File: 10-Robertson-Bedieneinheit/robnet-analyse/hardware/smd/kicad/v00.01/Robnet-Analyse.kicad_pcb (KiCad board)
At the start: 2 copper layers, 100 x 100 mm, 71 parts, among them J1 MSTBA 6-pol., J2 MSTBA 2-pol., J3 MSTBA 6-pol., J4 Messpunkte, J5 Raspberry Pi Zero 2 W, U1 MAX3488EEPA, U2 MCP3208-CI/P, U3 R-78B5.0-2.0, U4 LM4040AIZ-2.5, U6 MCP3208-CI/P

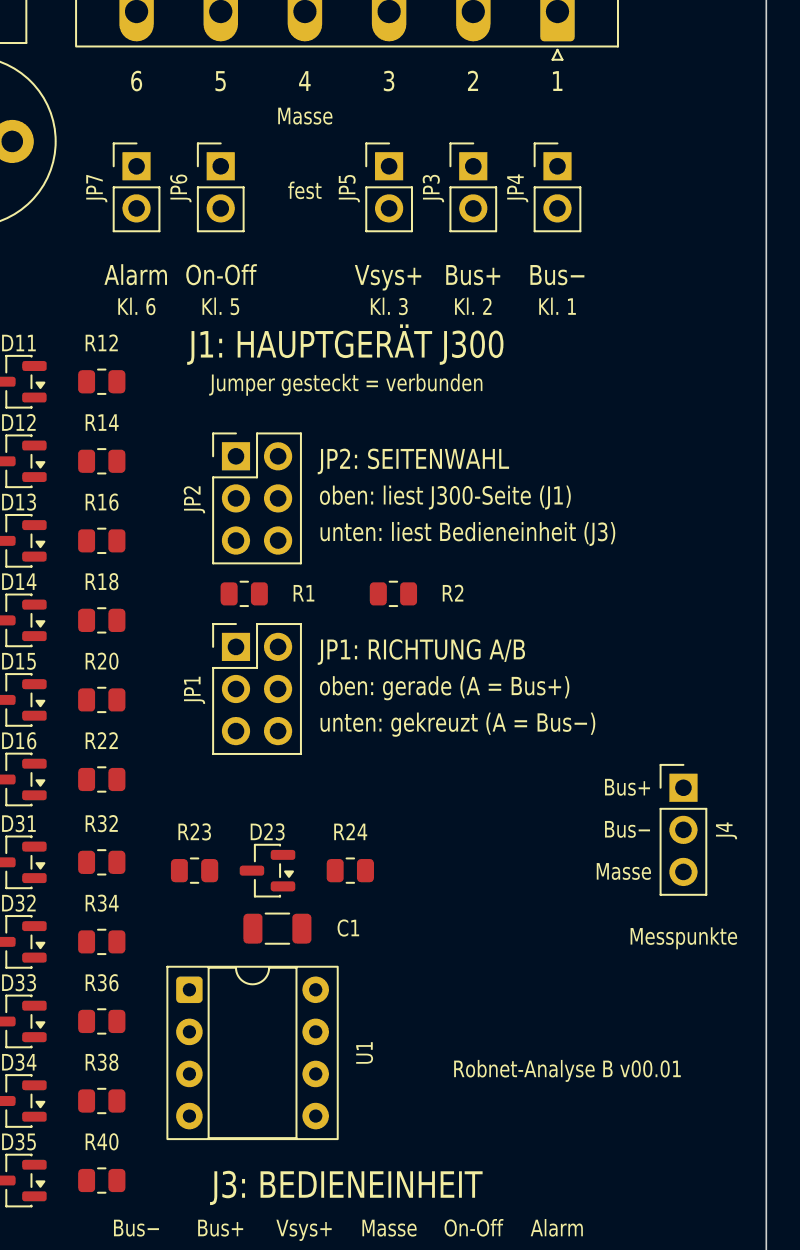
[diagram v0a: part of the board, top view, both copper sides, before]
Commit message: Robnet-Analyse Linie B: Aufdruck JP1/JP2 mit Stellungen A-E, Klemmennamen J1, Hersteller
- Jumper_JP1_JP2.html 00.01: alle Stellungen von JP1/JP2 (A-E) und falsche Steckungen
- Platine: Stiftreihen von JP1/JP2 beschriftet, Bildtabelle A-E und "nie quer",
  Klemmennamen an J1, "SuAn electronic" / "Lutz Pestel, 2026"
- Bauteilauswahl SMD 00.10, CLAUDE.md: Obergrenze 300 fuer die HTML-Seite

Co-Authored-By: Claude Opus 5.5 <noreply@anthropic.com>
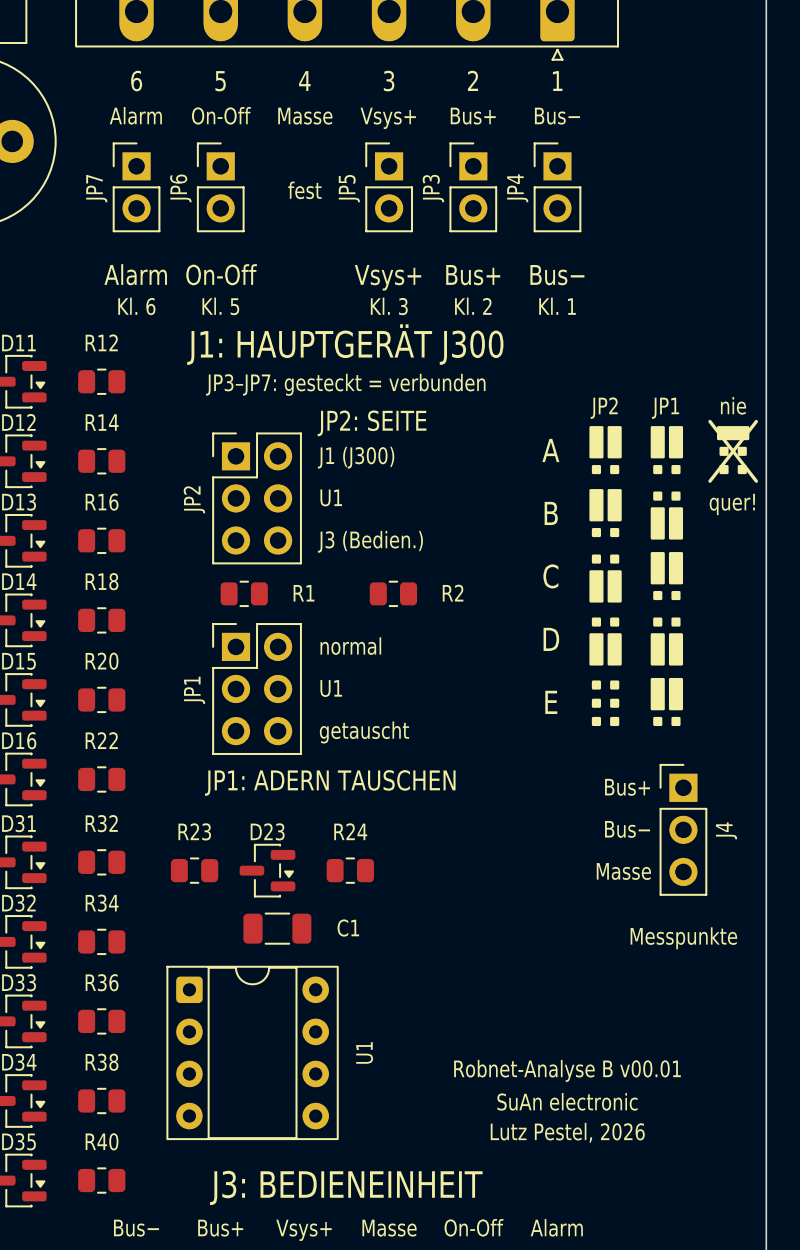
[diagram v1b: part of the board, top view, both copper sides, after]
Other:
- board text added: "A"
- board text added: "B"
- board text added: "C"
- board text added: "D"
- board text added: "E"
- board text added: "J1 (J300)"
- board text added: "J3 (Bedien.)"
- board text added: "JP1"
- board text added: "JP1: ADERN TAUSCHEN"
- board text added: "JP2"
- board text added: "JP2: SEITE"
- board text added: "JP3–JP7: gesteckt = verbunden"
- board text added: "Lutz Pestel, 2026"
- board text added: "SuAn electronic"
- board text added: "U1"
- board text added: "getauscht"
- board text added: "nie"
- board text added: "normal"
- board text added: "quer!"
- board text removed: "JP1: RICHTUNG A/B"
- board text removed: "JP2: SEITENWAHL"
- board text removed: "Jumper gesteckt = verbunden"
- board text removed: "oben: gerade (A = Bus+)"
- board text removed: "oben: liest J300-Seite (J1)"
- board text removed: "unten: gekreuzt (A = Bus−)"
- board text removed: "unten: liest Bedieneinheit (J3)"

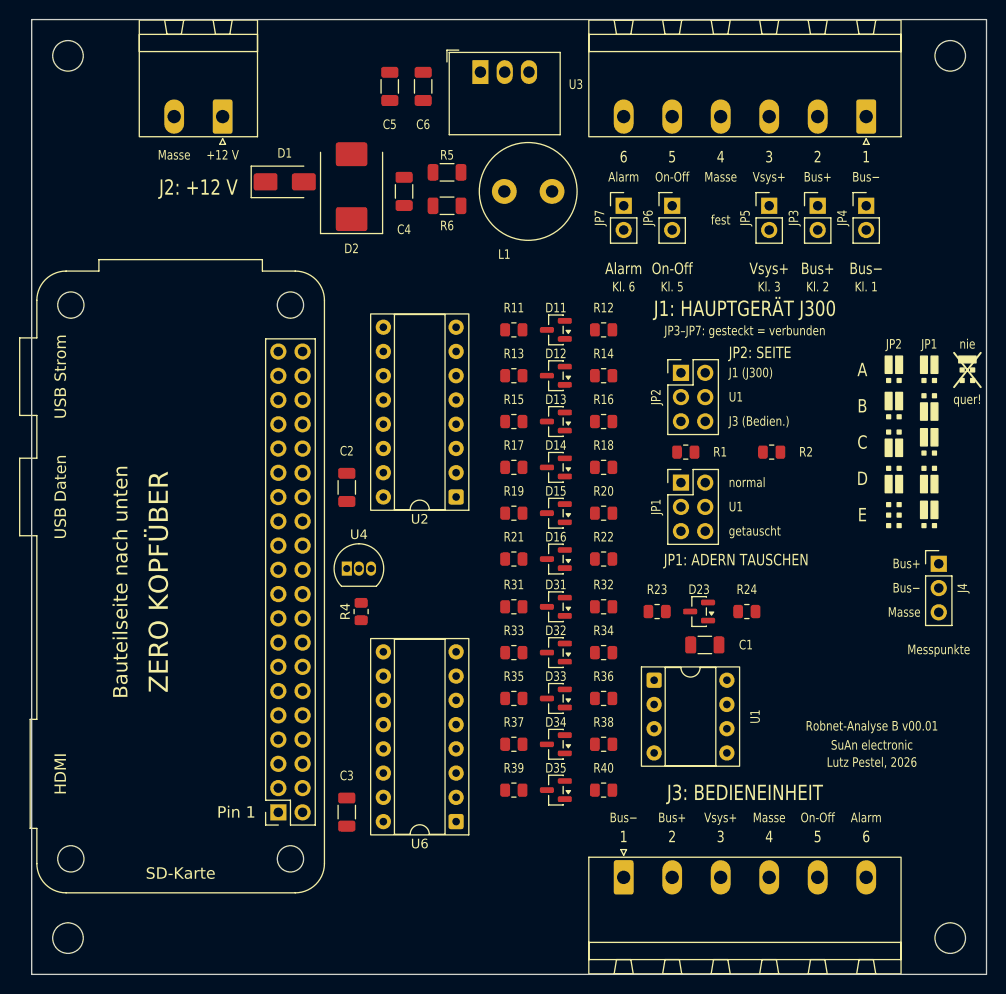
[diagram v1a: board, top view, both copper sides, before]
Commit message: Robnet-Analyse Linie B: Leiterbahnen Gruppe 1 (Versorgung und Masse)
- bahnen_erzeugen/robnet_bahnen.py 00.01: liest die platzierte Platine, ergaenzt Bahnen,
  bricht bei in KiCad verschobenen Teilen oder gezeichneten Bahnen ab
- Platzierungsskript 00.03 schreibt Zwischendatei Robnet-Analyse_platziert.kicad_pcb
  mit denselben Regeln; Projektdatei bleibt beim Speichern erhalten
- Gruppe 1: 12 V, 5 V aussen herum, 3,3 V unten mit Durchkontaktierung je BAT54S,
  Masseflaeche unten; DRC ohne Fehler, Abgleich 0; R21 (+12V_F) mit Gruppe 3
- Konzept 00.39, Bauteilauswahl SMD 00.11

Co-Authored-By: Claude Opus 5.5 <noreply@anthropic.com>
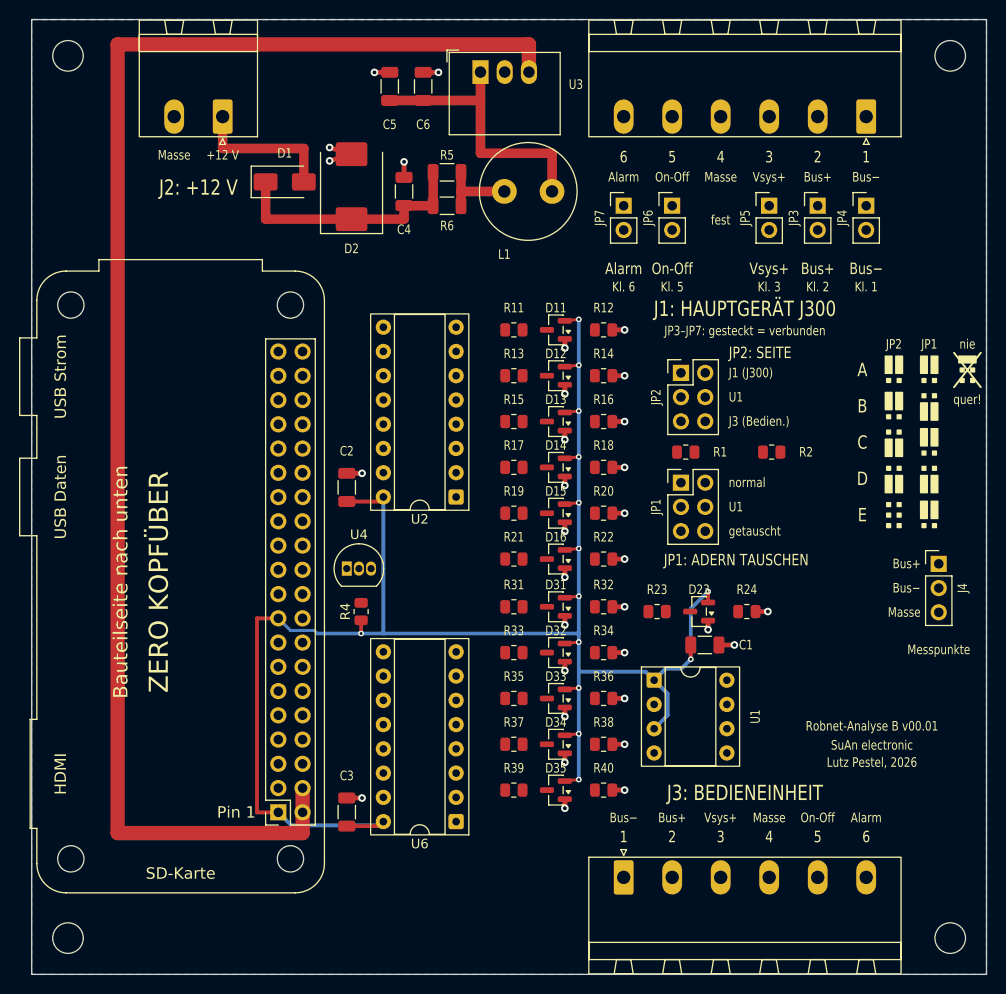
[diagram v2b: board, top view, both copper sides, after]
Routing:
- net /Bus-Empfänger/+3V3: track 0.00 -> 185.9 mm, vias 0 -> 14
- net /Rechner/+5V: track 0.00 -> 152.7 mm
- net GND: track 0.00 -> 41.3 mm, vias 0 -> 32
- net Net-(U3-IN): track 0.00 -> 29.5 mm
- net /Messung (Teiler, Wandler)/+12V_F: track 0.00 -> 26.3 mm
- net /Versorgung/+12V_EIN: track 0.00 -> 15.3 mm
- net Net-(L1-Pad1): track 0.00 -> 8.04 mm
- added copper zone on B.Cu, net GND

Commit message: Robnet-Analyse Linie B: Leiterbahnen Gruppe 2 (Adern J1 -> Jumper -> J3)
- Platzierung 00.04: R31-R39 um 180 Grad (Ader aussen), Kanalzeilen in Kanalfolge
  der Wandler (CH0 unten)
- Bahnen 00.02: Seite J300 ueber J1 und durch die Gasse zu den Teilern, Seite
  Bedieneinheit rechts herum und in Boegen unter J3 durch (keine Kreuzung trotz
  gespiegelter Klemmen); JP2, J4, R23, R21; 11 Durchkontaktierungen
- 3,3 V unten zwischen die Kanalbloecke verlegt; Schalter --neue-lage
- DRC ohne Fehler, Abgleich 0; Konzept 00.40, Bauteilauswahl SMD 00.12

Co-Authored-By: Claude Opus 5.5 <noreply@anthropic.com>
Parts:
- moved D11 24.0 mm to (54.9, 56.5)
- moved D16 24.0 mm to (54.9, 32.5)
- moved R11 24.0 mm to (50.5, 56.5)
- moved R12 24.0 mm to (59.9, 56.5)
- moved R21 24.0 mm to (50.5, 32.5)
- moved R22 24.0 mm to (59.9, 32.5)
- moved D31 19.2 mm to (54.9, 80.7)
- moved D35 19.2 mm to (54.9, 61.5)
- moved R31 19.2 mm to (50.5, 80.7), turned to 180 degrees
- moved R32 19.2 mm to (59.9, 80.7)
- moved R39 19.2 mm to (50.5, 61.5), turned to 180 degrees
- moved R40 19.2 mm to (59.9, 61.5)
- moved D12 14.4 mm to (54.9, 51.7)
- moved D15 14.4 mm to (54.9, 37.3)
- moved R13 14.4 mm to (50.5, 51.7)
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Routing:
- net /Bus-Empfänger/BUSN_J: track 0.00 -> 189.4 mm, vias 0 -> 2
- net /Bus-Empfänger/BUSN_B: track 0.00 -> 187.2 mm, vias 0 -> 1
- net /Bus-Empfänger/BUSP_B: track 0.00 -> 186.9 mm, vias 0 -> 1
- net /Bus-Empfänger/BUSP_J: track 0.00 -> 185.5 mm
- net /Messung (Teiler, Wandler)/ALARM_B: track 0.00 -> 157.4 mm, vias 0 -> 2
- net /Messung (Teiler, Wandler)/ONOFF_B: track 0.00 -> 153.2 mm, vias 0 -> 2
- net /Messung (Teiler, Wandler)/VSYS_B: track 0.00 -> 141.8 mm
- net /Messung (Teiler, Wandler)/ALARM_J: track 0.00 -> 107.8 mm, vias 0 -> 1
- net /Messung (Teiler, Wandler)/VSYS_J: track 0.00 -> 93.9 mm
- net /Messung (Teiler, Wandler)/ONOFF_J: track 0.00 -> 76.5 mm
- net /Messung (Teiler, Wandler)/+12V_F: track 26.3 -> 43.4 mm, vias 0 -> 2
- net /Bus-Empfänger/+3V3: track 185.9 -> 185.3 mm

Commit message: Robnet-Analyse Linie B: Leiterbahnen Gruppe 3 (Teiler -> Wandler, Referenz, Alarm)
- Bahnen 00.03: 11 Messleitungen oben kurz, unten ohne Kreuzung zu U2/U6;
  Referenz unten; Alarm zum Zero Pin 13 unten um U6 herum, Weg fuer die
  Empfaengerleitung frei
- 3,3 V an R4/U2 versetzt: Masseflaeche wieder ein Stueck
- DRC ohne Fehler, Abgleich 0; Konzept 00.41, Bauteilauswahl SMD 00.13

Co-Authored-By: Claude Opus 5.5 <noreply@anthropic.com>
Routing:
- net /Messung (Teiler, Wandler)/ALARM_ZERO: track 0.00 -> 104.0 mm, vias 0 -> 2
- net Net-(U2-Vref): track 0.00 -> 39.6 mm, vias 0 -> 1
- net Net-(D35-COM): track 0.00 -> 23.5 mm, vias 0 -> 1
- net Net-(D34-COM): track 0.00 -> 21.6 mm, vias 0 -> 1
- net Net-(D11-COM): track 0.00 -> 20.3 mm, vias 0 -> 1
- net /Bus-Empfänger/+3V3: track 185.3 -> 205.2 mm
- net Net-(D33-COM): track 0.00 -> 19.8 mm, vias 0 -> 1
- net Net-(D12-COM): track 0.00 -> 18.7 mm, vias 0 -> 1
- net Net-(D32-COM): track 0.00 -> 18.2 mm, vias 0 -> 1
- net Net-(D16-COM): track 0.00 -> 17.8 mm, vias 0 -> 1
- net Net-(D13-COM): track 0.00 -> 17.4 mm, vias 0 -> 1
- net Net-(D31-COM): track 0.00 -> 17.1 mm, vias 0 -> 1
- net Net-(D15-COM): track 0.00 -> 16.9 mm, vias 0 -> 1
- net Net-(D14-COM): track 0.00 -> 16.8 mm, vias 0 -> 1

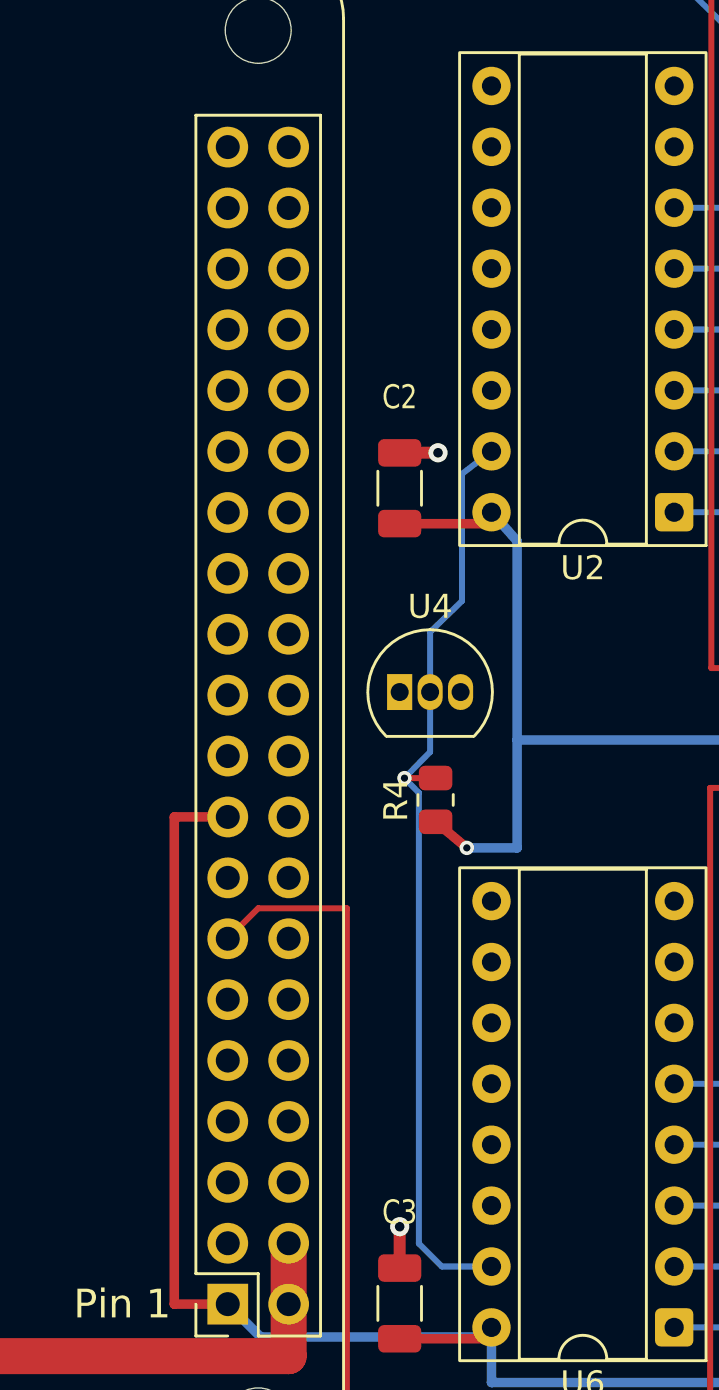
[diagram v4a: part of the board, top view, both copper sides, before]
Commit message: Robnet-Analyse Linie B: Leiterbahnen Gruppe 4 (SPI zum Zero)
- Bahnen 00.04: SPI unten waagerecht aus der Stiftleiste, je Ast eine
  Durchkontaktierung 0,5 mm, oben zu U2 hinauf und zu U6 hinunter ohne Kreuzung
- Referenz-Durchkontaktierung an R4 nach rechts
- DRC ohne Fehler, Abgleich 0; Konzept 00.42, Bauteilauswahl SMD 00.14

Co-Authored-By: Claude Opus 5.5 <noreply@anthropic.com>
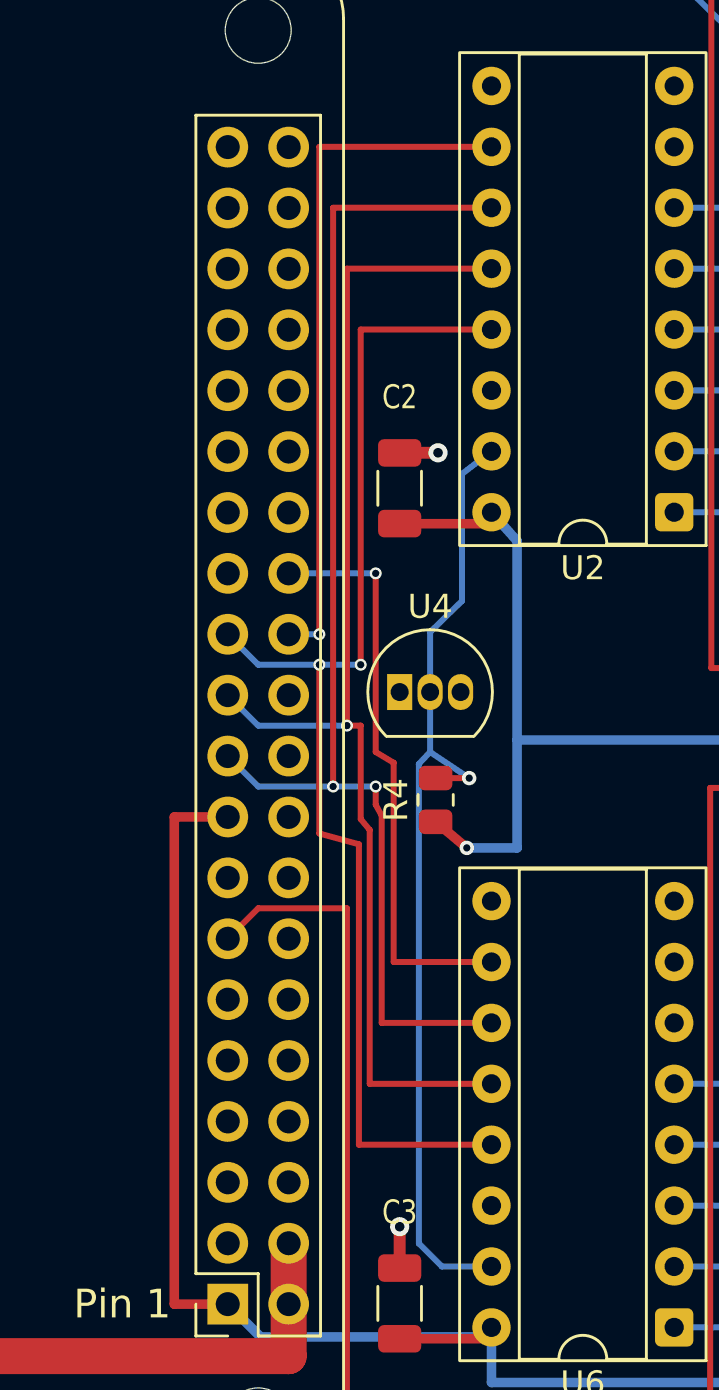
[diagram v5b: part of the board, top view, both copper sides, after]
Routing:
- net /Messung (Teiler, Wandler)/SCLK: track 0.00 -> 52.3 mm, vias 0 -> 2
- net /Messung (Teiler, Wandler)/MOSI: track 0.00 -> 51.9 mm, vias 0 -> 2
- net /Messung (Teiler, Wandler)/MISO: track 0.00 -> 51.3 mm, vias 0 -> 1
- net /Messung (Teiler, Wandler)/CE0: track 0.00 -> 28.8 mm, vias 0 -> 1
- net /Messung (Teiler, Wandler)/CE1: track 0.00 -> 24.3 mm, vias 0 -> 1
- net Net-(U2-Vref): track 39.6 -> 41.2 mm
